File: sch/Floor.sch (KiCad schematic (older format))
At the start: 12 parts, among them CON1 CTRL, CON2 PWR, Q1 MOSFET_N, Q2 MOSFET_N, Q3 MOSFET_N, Q4 MOSFET_N, Q5 MOSFET_N, Q6 MOSFET_N, Q7 MOSFET_N, Q8 MOSFET_N, U1 4017

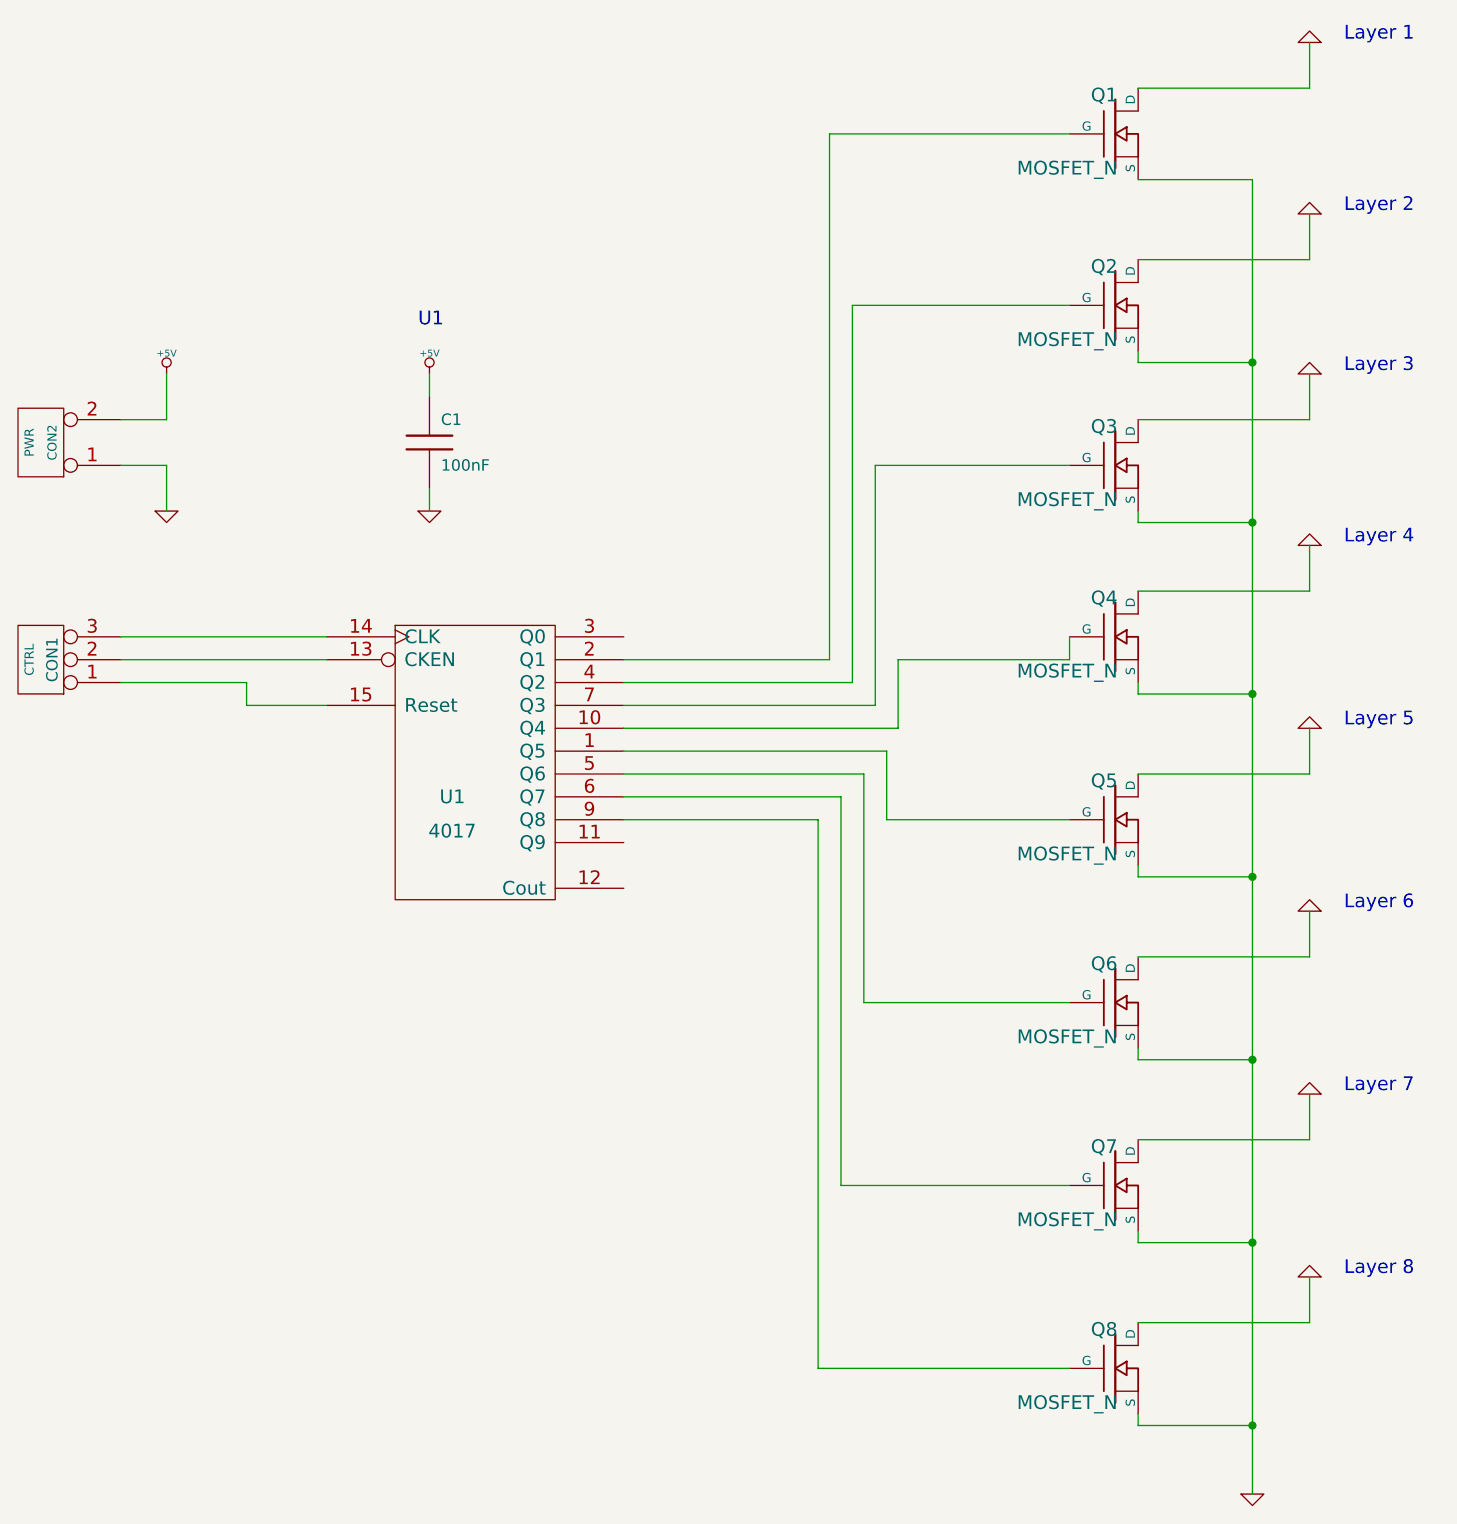
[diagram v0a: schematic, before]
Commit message: Updated some connections. Made the control sheet
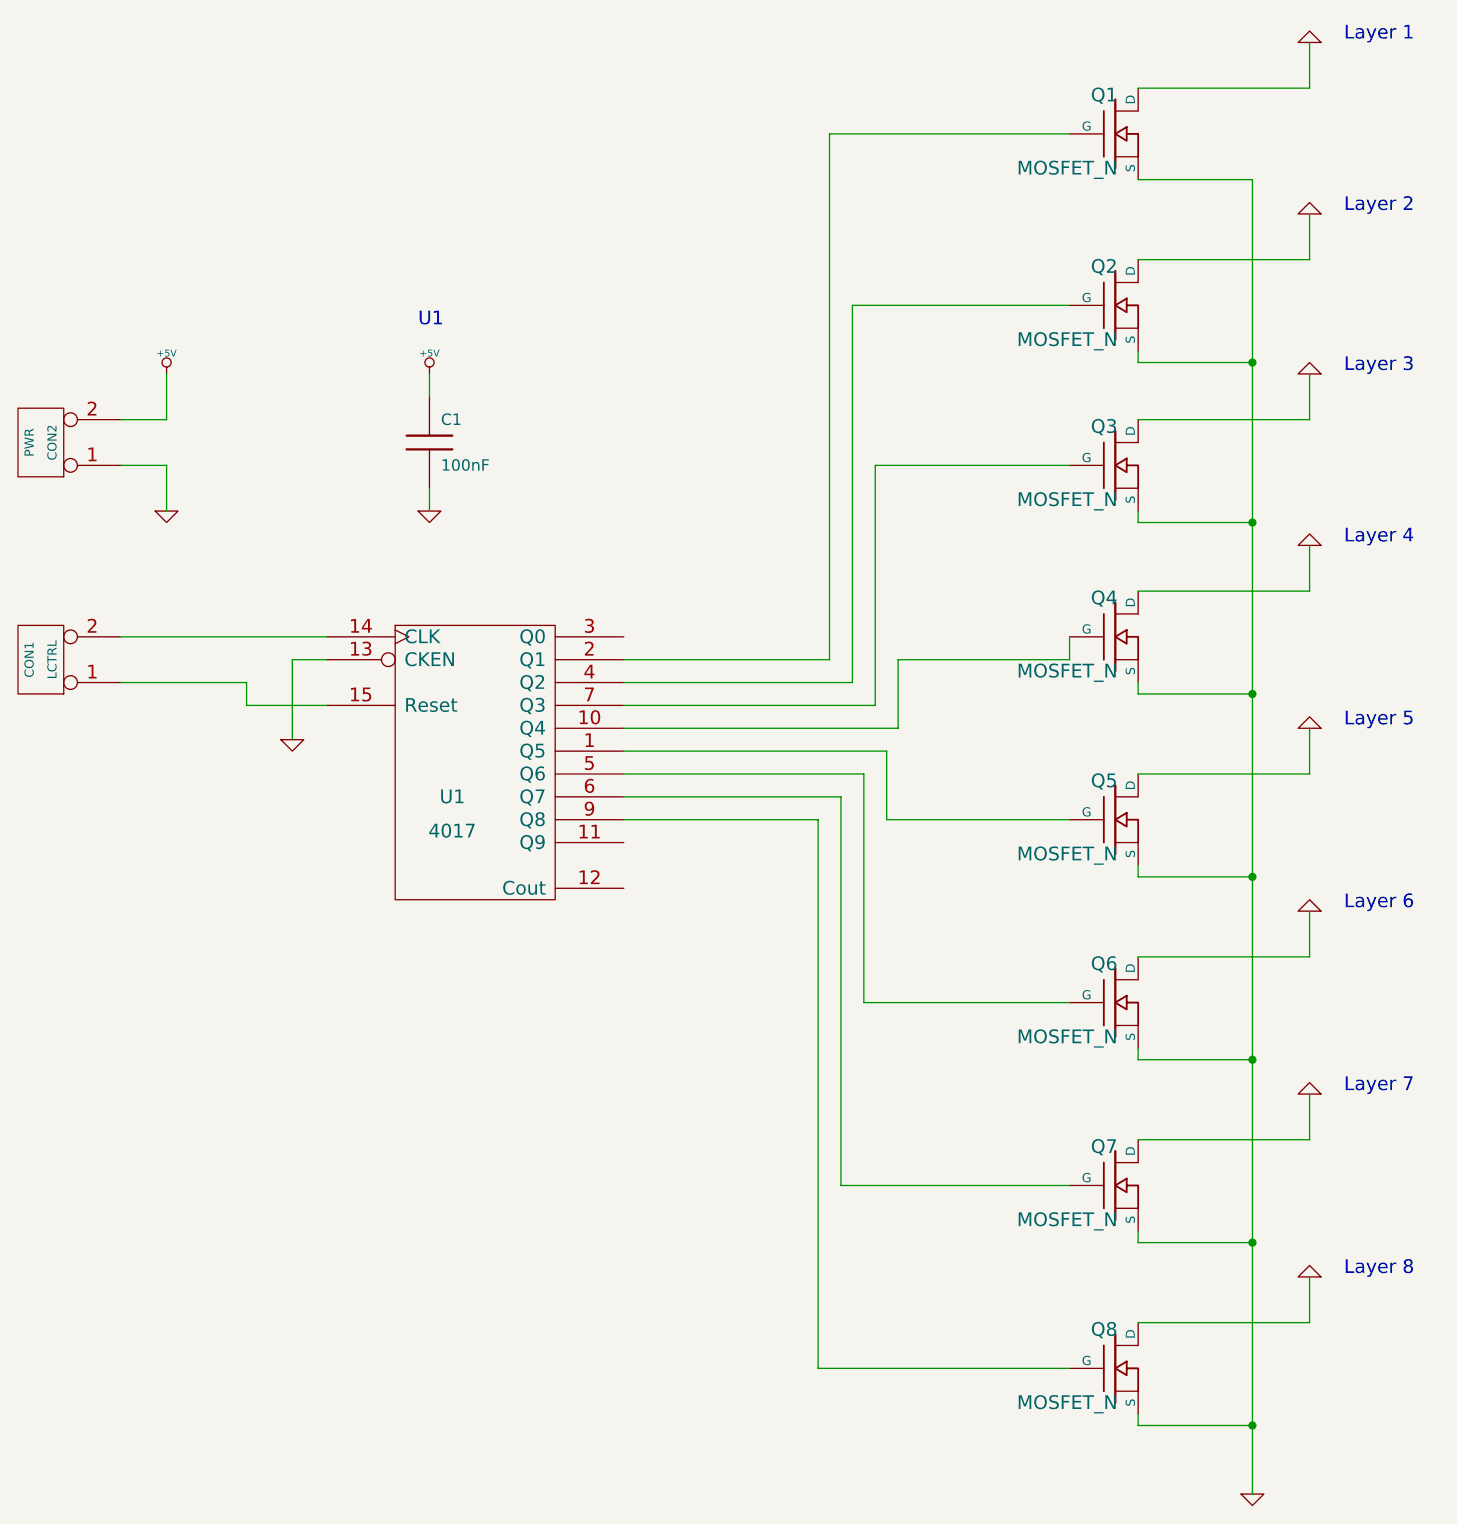
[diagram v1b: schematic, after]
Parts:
- removed CON1: CTRL, symbol CONN_3
- added LCTRL: CON1, symbol CONN_2
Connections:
- net GND: now also U1.13 (CKEN)
- net at U1.14 (CLK): now also LCTRL.2 (PM)
- net at U1.15 (Reset): now also LCTRL.1 (P1)
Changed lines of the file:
@@
-EESchema Schematic File Version 2  date Sat 26 Nov 2011 03:09:35 PM CET
+EESchema Schematic File Version 2  date Sat 03 Dec 2011 05:16:07 PM CET
 LIBS:power
 LIBS:device
@@
 $Descr A4 11700 8267
 encoding utf-8
-Sheet 2 4
+Sheet 3 4
 Title "Floor control"
-Date "26 nov 2011"
+Date "3 dec 2011"
 Rev "1.0"
 Comp ""
@@
 Comment4 ""
 $EndDescr
+Wire Wire Line
+	2250 3350 2400 3350
+Wire Wire Line
+	2250 3700 2250 3350
+Wire Wire Line
+	1500 3450 2050 3450
+Connection ~ 6450 6700
+Wire Wire Line
+	6450 6700 5950 6700
+Wire Wire Line
+	5950 6700 5950 6650
+Connection ~ 6450 5100
+Wire Wire Line
+	6450 5100 5950 5100
+Wire Wire Line
+	5950 5100 5950 5050
+Connection ~ 6450 3500
+Wire Wire Line
+	6450 3500 5950 3500
+Wire Wire Line
+	5950 3500 5950 3450
+Connection ~ 6450 2050
+Wire Wire Line
+	6450 2050 5950 2050
+Wire Wire Line
+	5950 2050 5950 2000
+Wire Wire Line
+	2850 2600 2850 2700
+Wire Wire Line
+	1700 2100 1700 2300
+Wire Wire Line
+	1700 2300 1500 2300
+Wire Wire Line
+	2400 3550 2050 3550
+Wire Wire Line
+	2050 3550 2050 3450
+Wire Wire Line
+	5650 5650 4650 5650
+Wire Wire Line
+	4650 5650 4650 3950
+Wire Wire Line
+	4650 3950 3700 3950
+Wire Wire Line
+	3700 3750 4850 3750
+Wire Wire Line
+	4850 3750 4850 4050
+Wire Wire Line
+	4850 4050 5650 4050
+Wire Wire Line
+	3700 3550 4800 3550
+Wire Wire Line
+	4800 3550 4800 2500
+Wire Wire Line
+	4800 2500 5650 2500
+Wire Wire Line
+	3700 3350 4600 3350
+Wire Wire Line
+	4600 3350 4600 1050
+Wire Wire Line
+	4600 1050 5650 1050
+Wire Wire Line
+	5650 1800 4700 1800
+Wire Wire Line
+	4700 1800 4700 3450
+Wire Wire Line
+	4700 3450 3700 3450
+Wire Wire Line
+	5650 3250 5650 3350
+Wire Wire Line
+	5650 3350 4900 3350
+Wire Wire Line
+	4900 3350 4900 3650
+Wire Wire Line
+	4900 3650 3700 3650
+Wire Wire Line
+	5650 4850 4750 4850
+Wire Wire Line
+	4750 4850 4750 3850
+Wire Wire Line
+	4750 3850 3700 3850
+Wire Wire Line
+	5650 6450 4550 6450
+Wire Wire Line
+	4550 6450 4550 4050
+Wire Wire Line
+	4550 4050 3700 4050
+Wire Wire Line
+	1500 2500 1700 2500
+Wire Wire Line
+	1700 2500 1700 2700
+Wire Wire Line
+	2850 2100 2850 2200
+Wire Wire Line
+	5950 1250 6450 1250
+Wire Wire Line
+	6450 1250 6450 7000
+Wire Wire Line
+	5950 2700 5950 2750
+Wire Wire Line
+	5950 2750 6450 2750
+Connection ~ 6450 2750
+Wire Wire Line
+	5950 4250 5950 4300
+Wire Wire Line
+	5950 4300 6450 4300
+Connection ~ 6450 4300
+Wire Wire Line
+	5950 5850 5950 5900
+Wire Wire Line
+	5950 5900 6450 5900
+Connection ~ 6450 5900
+Wire Wire Line
+	5950 1600 6700 1600
+Wire Wire Line
+	6700 1600 6700 1400
+Wire Wire Line
+	6700 650  6700 850
+Wire Wire Line
+	6700 850  5950 850
+Wire Wire Line
+	5950 2300 6700 2300
+Wire Wire Line
+	6700 2300 6700 2100
+Wire Wire Line
+	6700 2850 6700 3050
+Wire Wire Line
+	6700 3050 5950 3050
+Wire Wire Line
+	5950 6250 6700 6250
+Wire Wire Line
+	6700 6250 6700 6050
+Wire Wire Line
+	6700 5250 6700 5450
+Wire Wire Line
+	6700 5450 5950 5450
+Wire Wire Line
+	5950 3850 6700 3850
+Wire Wire Line
+	6700 3850 6700 3650
+Wire Wire Line
+	6700 4450 6700 4650
+Wire Wire Line
+	6700 4650 5950 4650
+Wire Wire Line
+	2400 3250 1500 3250
+$Comp
+L GND #PWR?
+U 1 1 4EDA4AB7
+P 2250 3700
+F 0 "#PWR?" H 2250 3700 30  0001 C CNN
+F 1 "GND" H 2250 3630 30  0001 C CNN
+	1    2250 3700
+	1    0    0    -1
+$EndComp
+$Comp
+L CONN_2 LCTRL
+U 1 1 4EDA4AA3
+P 1150 3350
+F 0 "LCTRL" V 1100 3350 40  0000 C CNN
+F 1 "CON1" V 1200 3350 40  0000 C CNN
+	1    1150 3350
+	-1   0    0    1
+$EndComp
 Text Notes 6850 6050 0    60   ~ 0
 Layer 8
@@
 	-1   0    0    1
 $EndComp
-Wire Wire Line
-	6700 4650 5950 4650
-Wire Wire Line
-	6700 4450 6700 4650
-Wire Wire Line
-	6700 3650 6700 3850
-Wire Wire Line
-	6700 3850 5950 3850
 $Comp
 L GND #PWR?
@@
 	-1   0    0    1
 $EndComp
-Wire Wire Line
-	6700 5450 5950 5450
-Wire Wire Line
-	6700 5250 6700 5450
-Wire Wire Line
-	6700 6050 6700 6250
-Wire Wire Line
-	6700 6250 5950 6250
 $Comp
 L GND #PWR?
@@
 	-1   0    0    1
 $EndComp
-Wire Wire Line
-	6700 3050 5950 3050
-Wire Wire Line
-	6700 2850 6700 3050
-Wire Wire Line
-	6700 2100 6700 2300
-Wire Wire Line
-	6700 2300 5950 2300
 $Comp
 L GND #PWR?
@@
 	-1   0    0    1
 $EndComp
-Wire Wire Line
-	6700 850  5950 850
-Wire Wire Line
-	6700 650  6700 850
-Wire Wire Line
-	6700 1400 6700 1600
-Wire Wire Line
-	6700 1600 5950 1600
-Connection ~ 6450 5900
-Wire Wire Line
-	6450 5900 5950 5900
-Wire Wire Line
-	5950 5900 5950 5850
-Connection ~ 6450 4300
-Wire Wire Line
-	6450 4300 5950 4300
-Wire Wire Line
-	5950 4300 5950 4250
-Connection ~ 6450 2750
-Wire Wire Line
-	6450 2750 5950 2750
-Wire Wire Line
-	5950 2750 5950 2700
-Wire Wire Line
-	6450 7000 6450 1250
-Wire Wire Line
-	6450 1250 5950 1250
-Wire Wire Line
-	2850 2100 2850 2200
-Wire Wire Line
-	1700 2700 1700 2500
-Wire Wire Line
-	1700 2500 1500 2500
-Wire Wire Line
-	2400 3350 1500 3350
-Wire Wire Line
-	3700 4050 4550 4050
-Wire Wire Line
-	4550 4050 4550 6450
-Wire Wire Line
-	4550 6450 5650 6450
-Wire Wire Line
-	3700 3850 4750 3850
-Wire Wire Line
-	4750 3850 4750 4850
-Wire Wire Line
-	4750 4850 5650 4850
-Wire Wire Line
-	3700 3650 4900 3650
-Wire Wire Line
-	4900 3650 4900 3350
-Wire Wire Line
-	4900 3350 5650 3350
-Wire Wire Line
-	5650 3350 5650 3250
-Wire Wire Line
-	3700 3450 4700 3450
-Wire Wire Line
-	4700 3450 4700 1800
-Wire Wire Line
-	4700 1800 5650 1800
-Wire Wire Line
-	5650 1050 4600 1050
-Wire Wire Line
-	4600 1050 4600 3350
-Wire Wire Line
-	4600 3350 3700 3350
-Wire Wire Line
-	5650 2500 4800 2500
-Wire Wire Line
-	4800 2500 4800 3550
-Wire Wire Line
-	4800 3550 3700 3550
-Wire Wire Line
-	5650 4050 4850 4050
-Wire Wire Line
-	4850 4050 4850 3750
-Wire Wire Line
-	4850 3750 3700 3750
-Wire Wire Line
-	3700 3950 4650 3950
-Wire Wire Line
-	4650 3950 4650 5650
-Wire Wire Line
-	4650 5650 5650 5650
-Wire Wire Line
-	1500 3250 2400 3250
-Wire Wire Line
-	1500 3450 2050 3450
-Wire Wire Line
-	2050 3450 2050 3550
-Wire Wire Line
-	2050 3550 2400 3550
-Wire Wire Line
-	1500 2300 1700 2300
-Wire Wire Line
-	1700 2300 1700 2100
-Wire Wire Line
-	2850 2600 2850 2700
-Wire Wire Line
-	5950 2000 5950 2050
-Wire Wire Line
-	5950 2050 6450 2050
-Connection ~ 6450 2050
-Wire Wire Line
-	5950 3450 5950 3500
-Wire Wire Line
-	5950 3500 6450 3500
-Connection ~ 6450 3500
-Wire Wire Line
-	5950 5050 5950 5100
-Wire Wire Line
-	5950 5100 6450 5100
-Connection ~ 6450 5100
-Wire Wire Line
-	5950 6650 5950 6700
-Wire Wire Line
-	5950 6700 6450 6700
-Connection ~ 6450 6700
 $Comp
 L GND #PWR?
@@
 	-1   0    0    1
 $EndComp
-$Comp
-L CONN_3 CON1
-U 1 1 4ECD1F2D
-P 1150 3350
-F 0 "CON1" V 1100 3350 50  0000 C CNN
-F 1 "CTRL" V 1200 3350 40  0000 C CNN
-	1    1150 3350
-	-1   0    0    1
-$EndComp
